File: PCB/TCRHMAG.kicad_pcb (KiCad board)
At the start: 2 copper layers, 45 x 36.1 mm, 3 parts, among them J1 CONN_LED, J2 CONN_THERM, SW1 PWR_SW

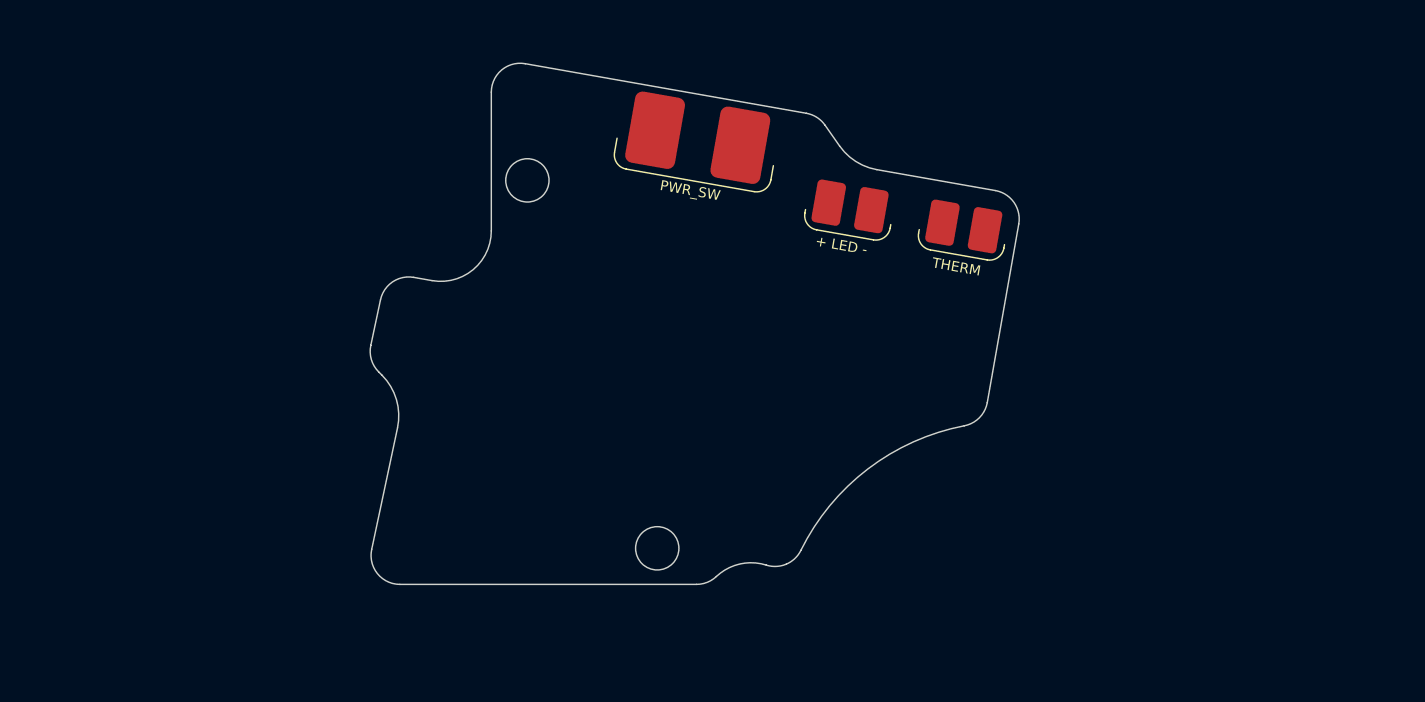
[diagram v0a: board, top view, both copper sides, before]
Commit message: PCB Components Chosen
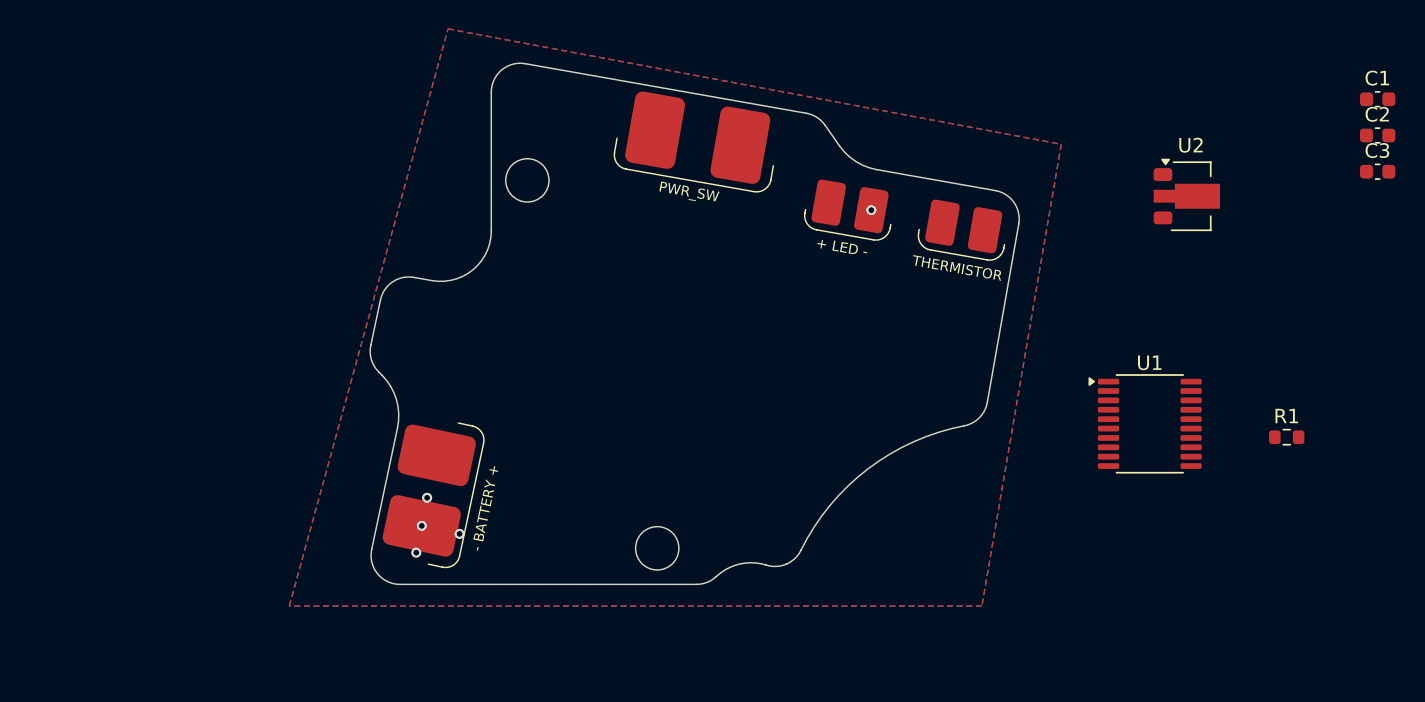
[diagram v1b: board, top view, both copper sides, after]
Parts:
- added C1: 100nF, Capacitor_SMD:C_0603_1608Metric, F.Cu at (134.9, 56.4)
- added C2: 10uF, Capacitor_SMD:C_0603_1608Metric, F.Cu at (134.9, 58.9)
- added C3: 100nF, Capacitor_SMD:C_0603_1608Metric, F.Cu at (134.9, 61.4)
- added J1: CONN_BATTERY, TCRHMAG:Power_Conn, F.Cu at (69.2, 83.5)
- added R1: 330R, Resistor_SMD:R_0603_1608Metric, F.Cu at (128.6, 79.8)
- added U1: CH32V003FxPx, Package_SO:TSSOP-20_4.4x6.5mm_P0.65mm, F.Cu at (119.1, 78.9)
- added U2: L78L05_SOT89, Package_TO_SOT_SMD:SOT-89-3, F.Cu at (122.0, 63.1)
- renumbered J1 to J2, J2 to J3
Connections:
- J2 pad 1: unconnected-(J1-Pin_1-Pad1) -> Net-(J2-Pin_1)
- J2 pad 2: unconnected-(J1-Pin_2-Pad2) -> GND
- SW1 pad 1: unconnected-(SW1-A-Pad1) -> Net-(J1-Pin_2)
- SW1 pad 2: unconnected-(SW1-B-Pad2) -> /PBUS_BATT
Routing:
- net GND: vias 0 -> 5
- added copper zone on B.Cu, net GND
- added copper zone on F.Cu, net GND
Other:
- board text added: "- BATTERY +"
- board text added: "THERMISTOR"
- board text removed: "THERM"

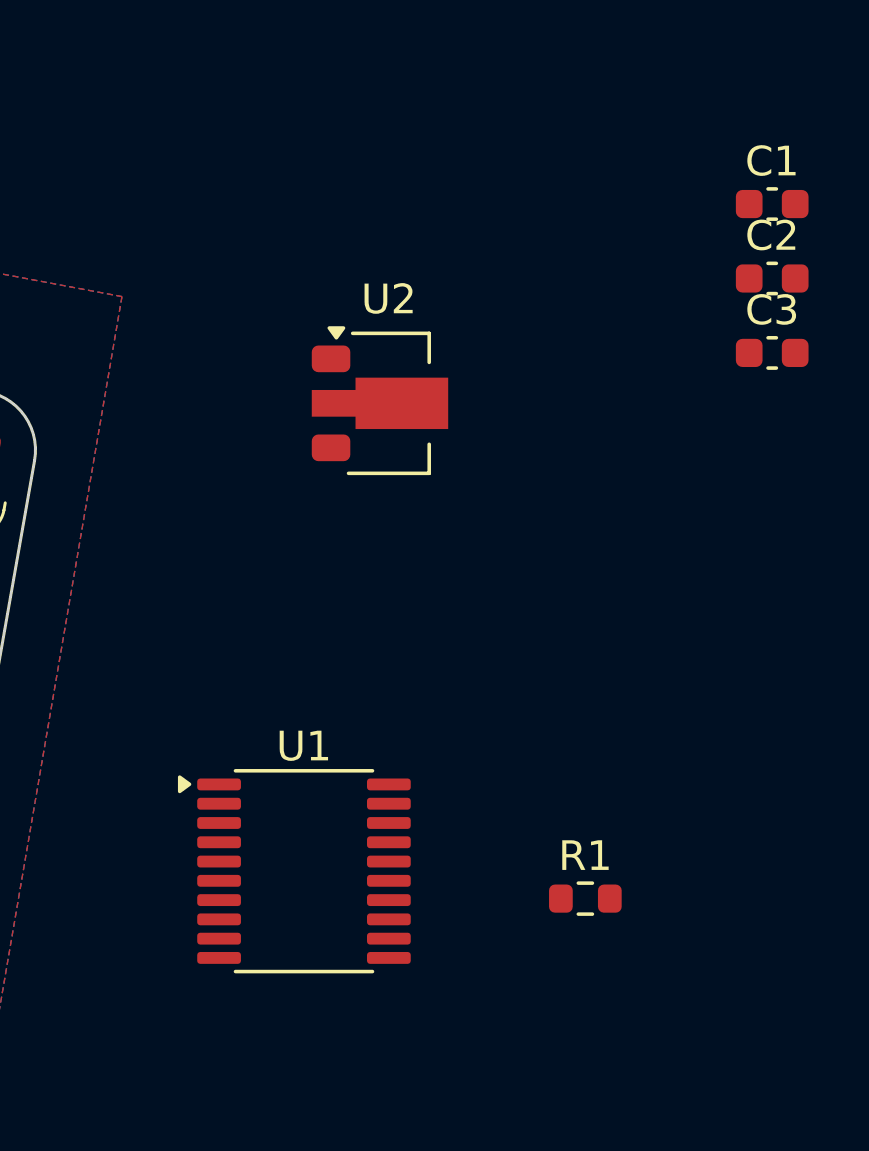
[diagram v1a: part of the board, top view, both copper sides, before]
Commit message: Board Shape and Pad Placements
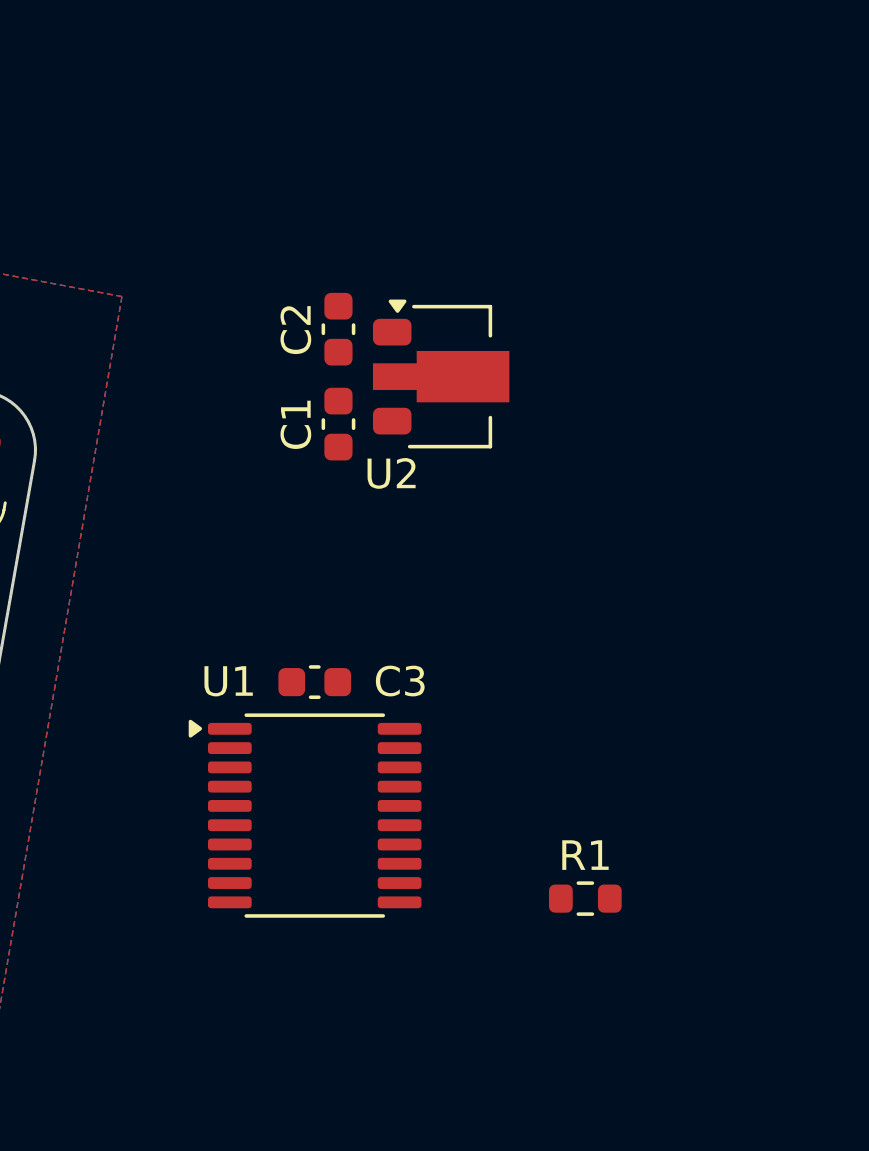
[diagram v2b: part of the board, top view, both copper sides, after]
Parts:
- moved C3 19.0 mm to (119.5, 72.5)
- moved C1 16.4 mm to (120.3, 63.8), turned to 90 degrees
- moved C2 14.7 mm to (120.3, 60.6), turned to -90 degrees
- moved U2 2.25 mm to (124.1, 62.2)
- moved U1 1.91 mm to (119.5, 77.0)
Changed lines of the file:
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@@
 	(footprint "Capacitor_SMD:C_0603_1608Metric"
 		(layer "F.Cu")
-		(at 134.925 61.4)
+		(at 119.5 72.5)
 		(descr "Capacitor SMD 0603 (1608 Metric), square (rectangular) end terminal, IPC-7351 nominal, (Body size source: IPC-SM-782 page 76, https://www.pcb-3d.com/wordpress/wp-content/uploads/ipc-sm-782a_amendment_1_and_2.pdf), generated with kicad-footprint-generator")
 		(tags "capacitor")
 		(property "Reference" "C3"
-			(at 0 -1.43 0)
+			(at 2.9 0 0)
 			(layer "F.SilkS")
 			(effects
@@
 		)
 		(property "Value" "100nF"
-			(at 0 1.43 0)
+			(at 4.4 0 0)
 			(layer "F.Fab")
 			(effects
@@
 	(footprint "Package_TO_SOT_SMD:SOT-89-3"
 		(layer "F.Cu")
-		(at 122 63.1)
+		(at 124.0625 62.2)
 		(descr "SOT-89-3, http://ww1.microchip.com/downloads/en/DeviceDoc/3L_SOT-89_MB_C04-029C.pdf")
 		(tags "SOT-89-3")
 		(property "Reference" "U2"
-			(at 0 -3.5 0)
+			(at -1.9625 3.3 0)
 			(layer "F.SilkS")
 			(effects
@@
 		)
 		(property "Value" "L78L05_SOT89"
-			(at 0 3.5 0)
+			(at 2.15 -10.35 0)
 			(layer "F.Fab")
 			(effects
@@
 	(footprint "Package_SO:TSSOP-20_4.4x6.5mm_P0.65mm"
 		(layer "F.Cu")
-		(at 119.1375 78.875)
+		(at 119.5 77)
 		(descr "TSSOP, 20 Pin (JEDEC MO-153 Var AC https://www.jedec.org/document_search?search_api_views_fulltext=MO-153), generated with kicad-footprint-generator ipc_gullwing_generator.py")
 		(tags "TSSOP SO")
 		(property "Reference" "U1"
-			(at 0 -4.2 0)
+			(at -2.9 -4.5 0)
 			(layer "F.SilkS")
 			(effects
@@
 	(footprint "Capacitor_SMD:C_0603_1608Metric"
 		(layer "F.Cu")
-		(at 134.925 56.38)
+		(at 120.3 63.8 90)
 		(descr "Capacitor SMD 0603 (1608 Metric), square (rectangular) end terminal, IPC-7351 nominal, (Body size source: IPC-SM-782 page 76, https://www.pcb-3d.com/wordpress/wp-content/uploads/ipc-sm-782a_amendment_1_and_2.pdf), generated with kicad-footprint-generator")
 		(tags "capacitor")
 		(property "Reference" "C1"
-			(at 0 -1.43 0)
+			(at 0 -1.4 90)
 			(layer "F.SilkS")
 			(effects
@@
 		)
 		(property "Value" "100nF"
-			(at 0 1.43 0)
+			(at 0 -1.4 90)
 			(layer "F.Fab")
 			(effects
@@
 		)
 		(property "Datasheet" "~"
-			(at 0 0 0)
+			(at 0 0 90)
 			(layer "F.Fab")
 			(hide yes)
@@
 		)
 		(property "Description" "Unpolarized capacitor"
-			(at 0 0 0)
+			(at 0 0 90)
 			(layer "F.Fab")
 			(hide yes)
@@
 		(attr smd)
 		(fp_line
-			(start -0.14058 -0.51)
-			(end 0.14058 -0.51)
-			(stroke
-				(width 0.12)
-				(type solid)
-			)
-			(layer "F.SilkS")
-		)
-		(fp_line
-			(start -0.14058 0.51)
-			(end 0.14058 0.51)
-			(stroke
-				(width 0.12)
-				(type solid)
-			)
-			(layer "F.SilkS")
-		)
-		(fp_rect
-			(start -1.48 -0.73)
-			(end 1.48 0.73)
+			(start -0.140581 -0.51)
+			(end 0.140581 -0.51)
+			(stroke
+				(width 0.12)
+				(type solid)
+			)
+			(layer "F.SilkS")
+		)
+		(fp_line
+			(start -0.140581 0.51)
+			(end 0.140581 0.51)
+			(stroke
+				(width 0.12)
+				(type solid)
+			)
+			(layer "F.SilkS")
+		)
+		(fp_poly
+			(pts
+				(xy -1.48 -0.73) (xy 1.48 -0.73) (xy 1.48 0.73) (xy -1.48 0.73)
+			)
 			(stroke
 				(width 0.05)
@@
 			(layer "F.CrtYd")
 		)
-		(fp_rect
-			(start -0.8 -0.4)
-			(end 0.8 0.4)
+		(fp_poly
+			(pts
+				(xy -0.8 -0.4) (xy 0.8 -0.4) (xy 0.8 0.4) (xy -0.8 0.4)
+			)
 			(stroke
 				(width 0.1)
@@
 		)
 		(fp_text user "${REFERENCE}"
-			(at 0 0 0)
+			(at 0 0 90)
 			(layer "F.Fab")
 			(effects
@@
 		)
 		(pad "1" smd roundrect
-			(at -0.775 0)
+			(at -0.775 0 90)
 			(size 0.9 0.95)
 			(layers "F.Cu" "F.Mask" "F.Paste")
@@
 		)
 		(pad "2" smd roundrect
-			(at 0.775 0)
+			(at 0.775 0 90)
 			(size 0.9 0.95)
 			(layers "F.Cu" "F.Mask" "F.Paste")
@@
 	(footprint "Capacitor_SMD:C_0603_1608Metric"
 		(layer "F.Cu")
-		(at 134.925 58.89)
+		(at 120.3 60.6 -90)
 		(descr "Capacitor SMD 0603 (1608 Metric), square (rectangular) end terminal, IPC-7351 nominal, (Body size source: IPC-SM-782 page 76, https://www.pcb-3d.com/wordpress/wp-content/uploads/ipc-sm-782a_amendment_1_and_2.pdf), generated with kicad-footprint-generator")
 		(tags "capacitor")
 		(property "Reference" "C2"
-			(at 0 -1.43 0)
+			(at 0 1.4 90)
 			(layer "F.SilkS")
 			(effects
@@
 		)
 		(property "Value" "10uF"
-			(at 0 1.43 0)
+			(at 0 1.4 90)
 			(layer "F.Fab")
 			(effects
@@
 		)
 		(property "Datasheet" "~"
-			(at 0 0 0)
+			(at 0 0 90)
 			(layer "F.Fab")
 			(hide yes)
@@
 		)
 		(property "Description" "Unpolarized capacitor"
-			(at 0 0 0)
+			(at 0 0 90)
 			(layer "F.Fab")
 			(hide yes)
@@
 		(attr smd)
 		(fp_line
-			(start -0.14058 -0.51)
-			(end 0.14058 -0.51)
-			(stroke
-				(width 0.12)
-				(type solid)
-			)
-			(layer "F.SilkS")
-		)
-		(fp_line
-			(start -0.14058 0.51)
-			(end 0.14058 0.51)
-			(stroke
-				(width 0.12)
-				(type solid)
-			)
-			(layer "F.SilkS")
-		)
-		(fp_rect
-			(start -1.48 -0.73)
-			(end 1.48 0.73)
+			(start -0.140581 0.51)
+			(end 0.140581 0.51)
+			(stroke
+				(width 0.12)
+				(type solid)
+			)
+			(layer "F.SilkS")
+		)
+		(fp_line
+			(start -0.140581 -0.51)
+			(end 0.140581 -0.51)
+			(stroke
+				(width 0.12)
+				(type solid)
+			)
+			(layer "F.SilkS")
+		)
+		(fp_poly
+			(pts
+				(xy -1.48 -0.73) (xy 1.48 -0.73) (xy 1.48 0.73) (xy -1.48 0.73)
+			)
 			(stroke
 				(width 0.05)
@@
 			(layer "F.CrtYd")
 		)
-		(fp_rect
-			(start -0.8 -0.4)
-			(end 0.8 0.4)
+		(fp_poly
+			(pts
+				(xy -0.8 -0.4) (xy 0.8 -0.4) (xy 0.8 0.4) (xy -0.8 0.4)
+			)
 			(stroke
 				(width 0.1)
@@
 		)
 		(fp_text user "${REFERENCE}"
-			(at 0 0 0)
+			(at 0 0 90)
 			(layer "F.Fab")
 			(effects
@@
 		)
 		(pad "1" smd roundrect
-			(at -0.775 0)
+			(at -0.775 0 270)
 			(size 0.9 0.95)
 			(layers "F.Cu" "F.Mask" "F.Paste")
@@
 		)
 		(pad "2" smd roundrect
-			(at 0.775 0)
+			(at 0.775 0 270)
 			(size 0.9 0.95)
 			(layers "F.Cu" "F.Mask" "F.Paste")

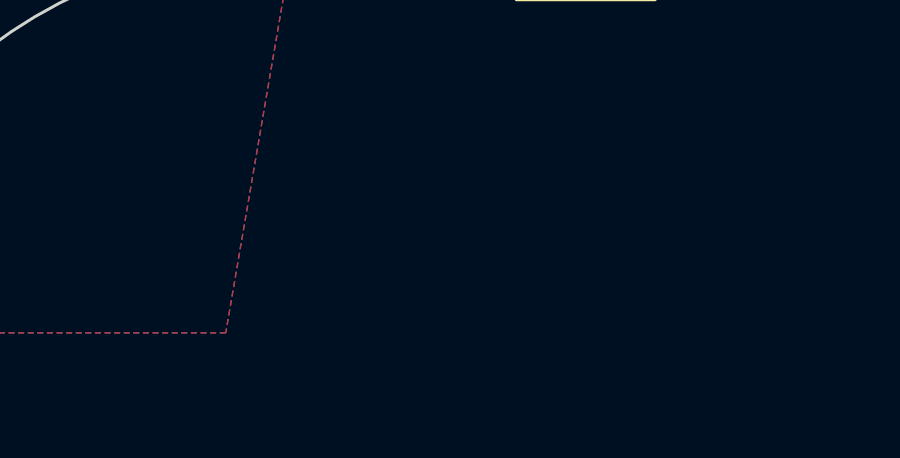
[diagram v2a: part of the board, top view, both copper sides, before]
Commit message: Added Current Sense to circuit
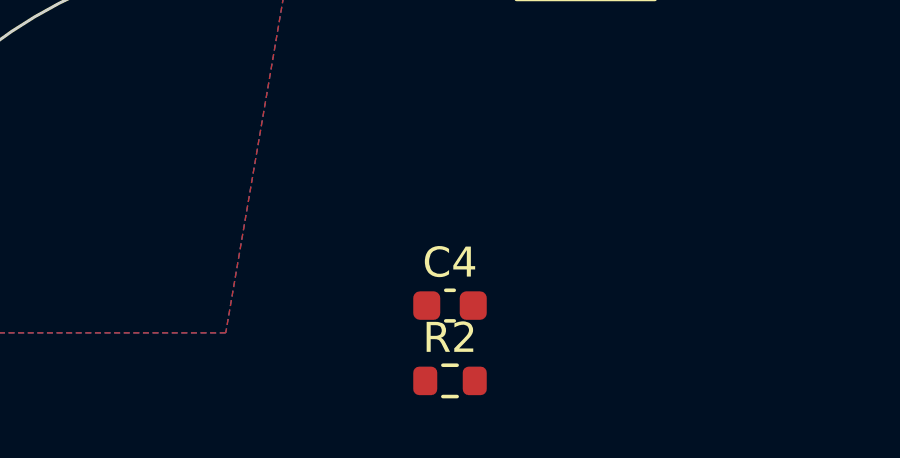
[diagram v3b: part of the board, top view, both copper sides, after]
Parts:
- added C4: 1uF, Capacitor_SMD:C_0603_1608Metric, F.Cu at (115.0, 90.6)
- added R2: 4K7, Resistor_SMD:R_0603_1608Metric, F.Cu at (115.0, 93.1)
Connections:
- J3 pad 1: unconnected-(J3-Pin_1-Pad1) -> /MCU_THERM_IN
- J3 pad 2: unconnected-(J3-Pin_2-Pad2) -> GND
